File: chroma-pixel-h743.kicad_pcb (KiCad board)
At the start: 6 copper layers, 76 x 78 mm, 136 parts, among them J1 Micro_SD_Card_Det_Hirose_DM3AT, J2 TFT_LCD, J4 USB-C, J5 I2C-STEMMA-QT, J6 BAT, J7 swd, J8 SPKR, J9 UART, SW1 SW_Push, SW2 SW_Push, SW3 SW_Push, SW4 SW_Push, U1 MT25Q, U10 STM32H743ZITx, U11 MT48LC16M16A2P, U5 TPS61169, U6 MAX98357AETE_, U7 CAT24C128, U8 TLV75733PDBV, U9 W25Q128JVS, Y1 25MHz, Y2 32.768KHz

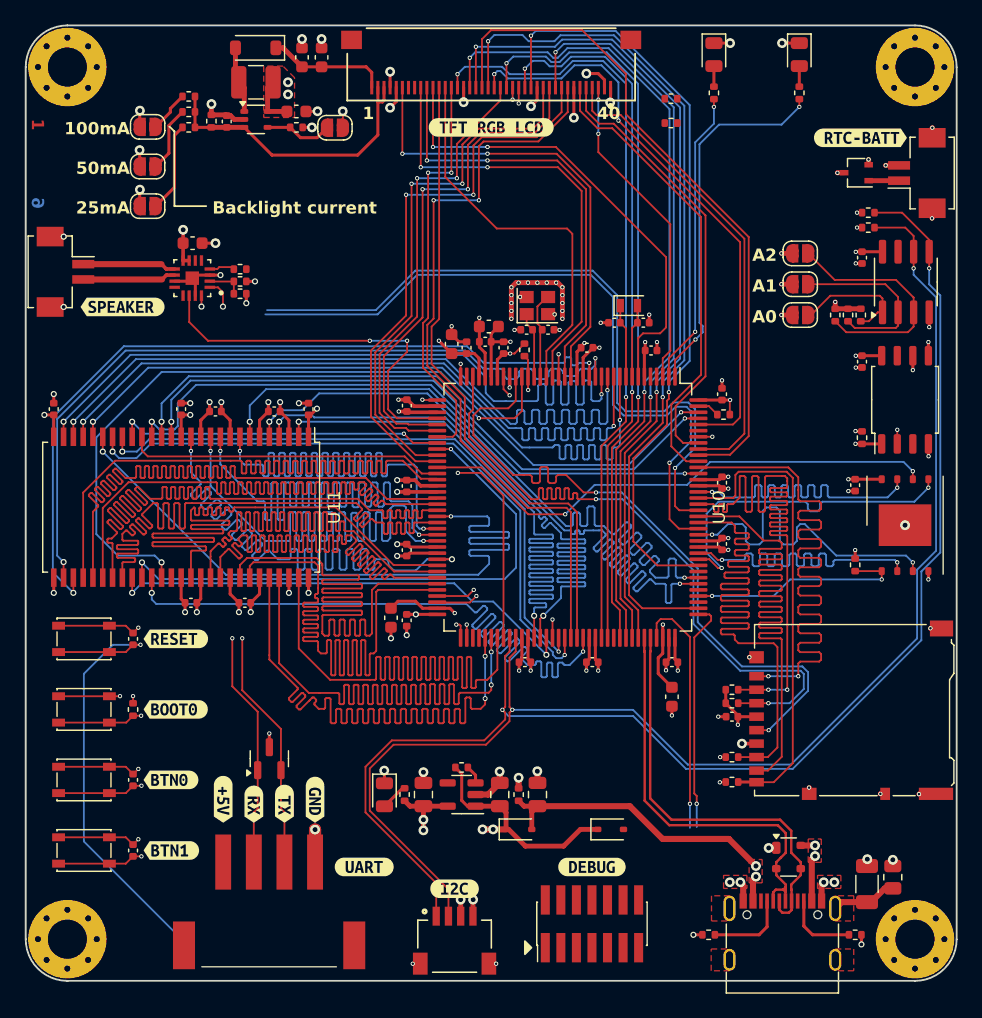
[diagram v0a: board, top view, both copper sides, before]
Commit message: LTDC route almost finished
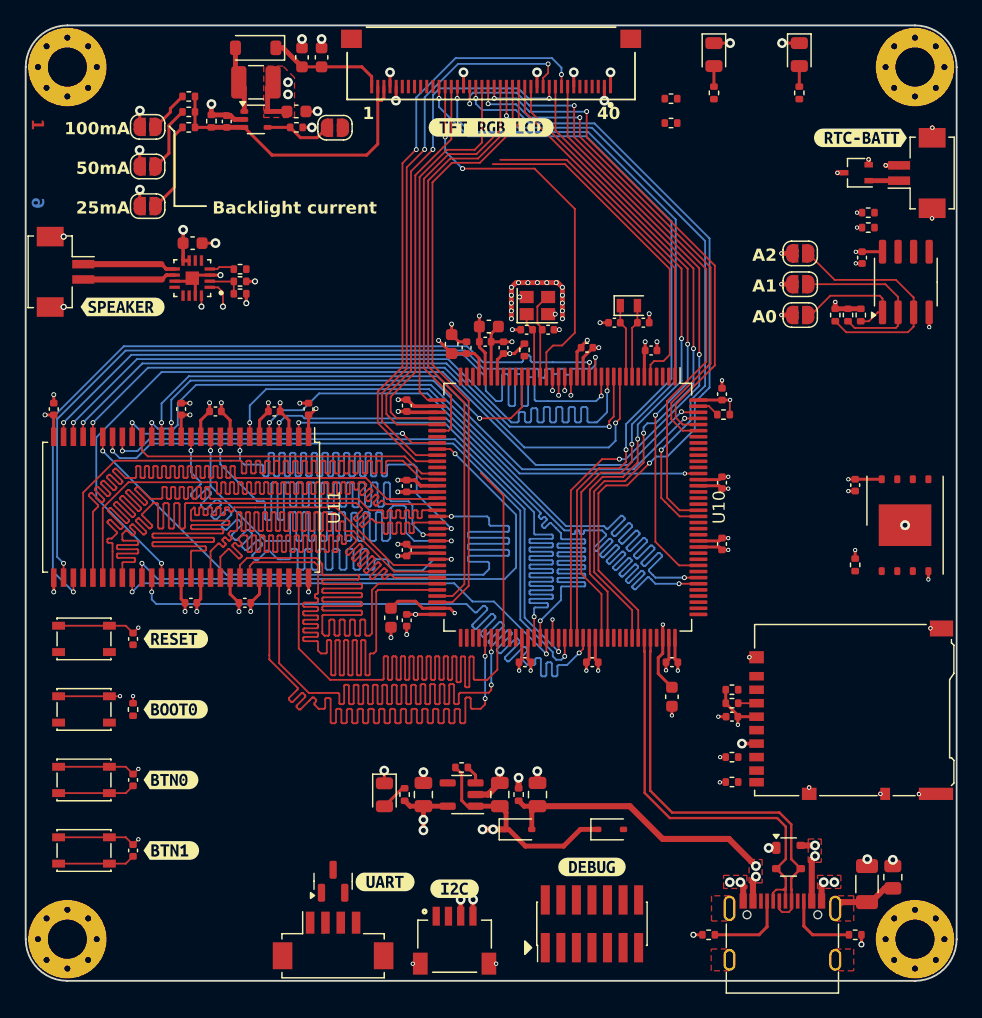
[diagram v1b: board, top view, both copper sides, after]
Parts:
- removed C22: 100n, Capacitor_SMD:C_0402_1005Metric
- removed R1: 10K, Resistor_SMD:R_0402_1005Metric
- removed U9: W25Q128JVS, Package_SO:SOIC-8_5.23x5.23mm_P1.27mm
- removed kibuzzard-664329E8: G***, kibuzzard-664329E8
- removed kibuzzard-664329F6: G***, kibuzzard-664329F6
- removed kibuzzard-6644A120: G***, kibuzzard-6644A120
- removed kibuzzard-6644A126: G***, kibuzzard-6644A126
- J9: footprint S4B-XH-SM4-TB_LF__SN:S4BXHSM4TBLFSN -> Connector_Hirose:Hirose_DF13C_CL535-0404-8-51_1x04-1MP_P1.25mm_Vertical
- moved D9 11.3 mm to (131.3, 118.2)
- moved J9 5.64 mm to (131.3, 123.0)
- moved kibuzzard-6642BE54 2.09 mm to (135.5, 118.3)
- moved J2 0.09 mm to (144.2, 51.4)
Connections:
- net /MCU/I2S_CK renamed /Audio/I2S_CK
- net /MCU/I2S_SDO renamed /Audio/I2S_SDO
- net /MCU/I2S_SD_MODE renamed /Audio/I2S_SD_MODE
- net /MCU/I2S_WS renamed /Audio/I2S_WS
- net /MCU/PC0 renamed /MCU/~{SDRAM_WE}
- net /MCU/PC4 renamed /MCU/~{SDRAM_CS}
- net /MCU/PC5 renamed /MCU/SDRAM_CKE
- net /MCU/PE0 renamed /MCU/SDRAM_LDQM
- net /MCU/PE1 renamed /MCU/SDRAM_UDQM
- net /MCU/PF11 renamed /MCU/~{SDRAM_RAS}
- net /MCU/PG15 renamed /MCU/~{SDRAM_CAS}
- net /MCU/PG4 renamed /MCU/SDRAM_BA0
- net /MCU/PG5 renamed /MCU/SDRAM_BA1
- net /MCU/PG8 renamed /MCU/SDRAM_CLK
- R2 pad 2: /MCU/~{NOR_CS} -> /MEMORY/~{NOR_CS}
- U1 pad 1: /MCU/~{NOR_CS} -> /MEMORY/~{NOR_CS}
- U1 pad 2: /MCU/NOR_D1 -> /MEMORY/NOR_DO(IO1)
- U1 pad 3: /MCU/NOR_D2 -> /MEMORY/NOR_IO2
- U1 pad 5: /MCU/NOR_D0 -> /MEMORY/NOR_DI(IO0)
- U1 pad 6: /MCU/NOR_CLK -> /MEMORY/NOR_CLK
- U1 pad 7: /MCU/NOR_D3 -> /MEMORY/NOR_IO3
- U10 pad 1: unconnected-(U10-PE2-Pad1) -> /LCD/LCD_SPI_CLK
- U10 pad 101: unconnected-(U10-PA9-Pad101) -> /LCD/LCD_R5
- U10 pad 102: unconnected-(U10-PA10-Pad102) -> /LCD/LCD_B4
- U10 pad 103: unconnected-(U10-PA11-Pad103) -> /MCU/USB_D-
- U10 pad 104: unconnected-(U10-PA12-Pad104) -> /MCU/USB_D+
- U10 pad 117: unconnected-(U10-PD3-Pad117) -> /LCD/LCD_G7
- U10 pad 125: unconnected-(U10-PG10-Pad125) -> /LCD/LCD_G3
- U10 pad 126: unconnected-(U10-PG11-Pad126) -> /LCD/LCD_B3
- U10 pad 136: unconnected-(U10-PB6-Pad136) -> /MEMORY/~{NOR_CS}
- U10 pad 139: unconnected-(U10-PB8-Pad139) -> /LCD/LCD_B6
- U10 pad 140: unconnected-(U10-PB9-Pad140) -> /LCD/LCD_B7
- U10 pad 18: unconnected-(U10-PF6-Pad18) -> /MEMORY/NOR_IO3
- U10 pad 19: unconnected-(U10-PF7-Pad19) -> /MEMORY/NOR_IO2
- U10 pad 2: unconnected-(U10-PE3-Pad2) -> /LCD/LCD_SPI_CS
- U10 pad 20: unconnected-(U10-PF8-Pad20) -> /MEMORY/NOR_DI(IO0)
- U10 pad 21: unconnected-(U10-PF9-Pad21) -> /MEMORY/NOR_DO(IO1)
- U10 pad 22: unconnected-(U10-PF10-Pad22) -> /LCD/LCD_DE
- U10 pad 3: unconnected-(U10-PE4-Pad3) -> /LCD/LCD_RESET
- U10 pad 37: unconnected-(U10-PA3-Pad37) -> /LCD/LCD_B5
- U10 pad 40: unconnected-(U10-PA4-Pad40) -> /LCD/VSYNC
- U10 pad 41: unconnected-(U10-PA5-Pad41) -> /LCD/LCD_R4
- U10 pad 42: unconnected-(U10-PA6-Pad42) -> /LCD/LCD_G2
- U10 pad 43: unconnected-(U10-PA7-Pad43) -> /LCD/LCD_BLK
- U10 pad 46: unconnected-(U10-PB0-Pad46) -> /LCD/LCD_R3
- U10 pad 47: unconnected-(U10-PB1-Pad47) -> /LCD/LCD_R6
- U10 pad 48: unconnected-(U10-PB2-Pad48) -> /MEMORY/NOR_CLK
- U10 pad 5: unconnected-(U10-PE6-Pad5) -> /LCD/LCD_SPI_DAT
- U10 pad 69: unconnected-(U10-PB10-Pad69) -> /LCD/LCD_G4
- U10 pad 70: unconnected-(U10-PB11-Pad70) -> /LCD/LCD_G5
- U10 pad 91: unconnected-(U10-PG6-Pad91) -> /LCD/LCD_R7
- U10 pad 92: unconnected-(U10-PG7-Pad92) -> /LCD/LCD_CLK
- U10 pad 96: unconnected-(U10-PC6-Pad96) -> /LCD/HSYNC
- U10 pad 97: unconnected-(U10-PC7-Pad97) -> /LCD/LCD_G6
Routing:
- net /IO/STEMMA_SCL: track 114.3 -> 0.00 mm, vias 2 -> 0
- net /IO/STEMMA_SDA: track 111.8 -> 0.00 mm, vias 2 -> 0
- net /IO/NRST: track 89.2 -> 0.00 mm, vias 2 -> 0
- net /MCU/BOOT0: track 72.3 -> 0.00 mm, vias 2 -> 0
- net /IO/USART2_TX: track 62.3 -> 0.00 mm, vias 2 -> 0
- net /MCU/SD_DAT0: track 60.5 -> 0.00 mm
- net /IO/USART2_RX: track 60.4 -> 0.00 mm, vias 2 -> 0
- net /MCU/SD_DAT3: track 59.9 -> 0.00 mm, vias 2 -> 0
- net /MCU/SD_DAT1: track 59.0 -> 0.00 mm
- net unconnected-(U10-PD7-Pad123): track 58.7 -> 0.00 mm, vias 1 -> 0
- net /MCU/SD_DAT2: track 58.4 -> 0.00 mm, vias 2 -> 0
- net /MCU/SPI_CLK: track 58.3 -> 0.00 mm, vias 2 -> 0
- net unconnected-(U10-PG11-Pad126): track 57.4 -> 0.00 mm, vias 1 -> 0
- net /MCU/SD_CMD: track 57.4 -> 1.50 mm, vias 2 -> 0
- net /MCU/SD_CLK: track 55.9 -> 0.00 mm, vias 2 -> 0
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
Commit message: Added chroma pixel png
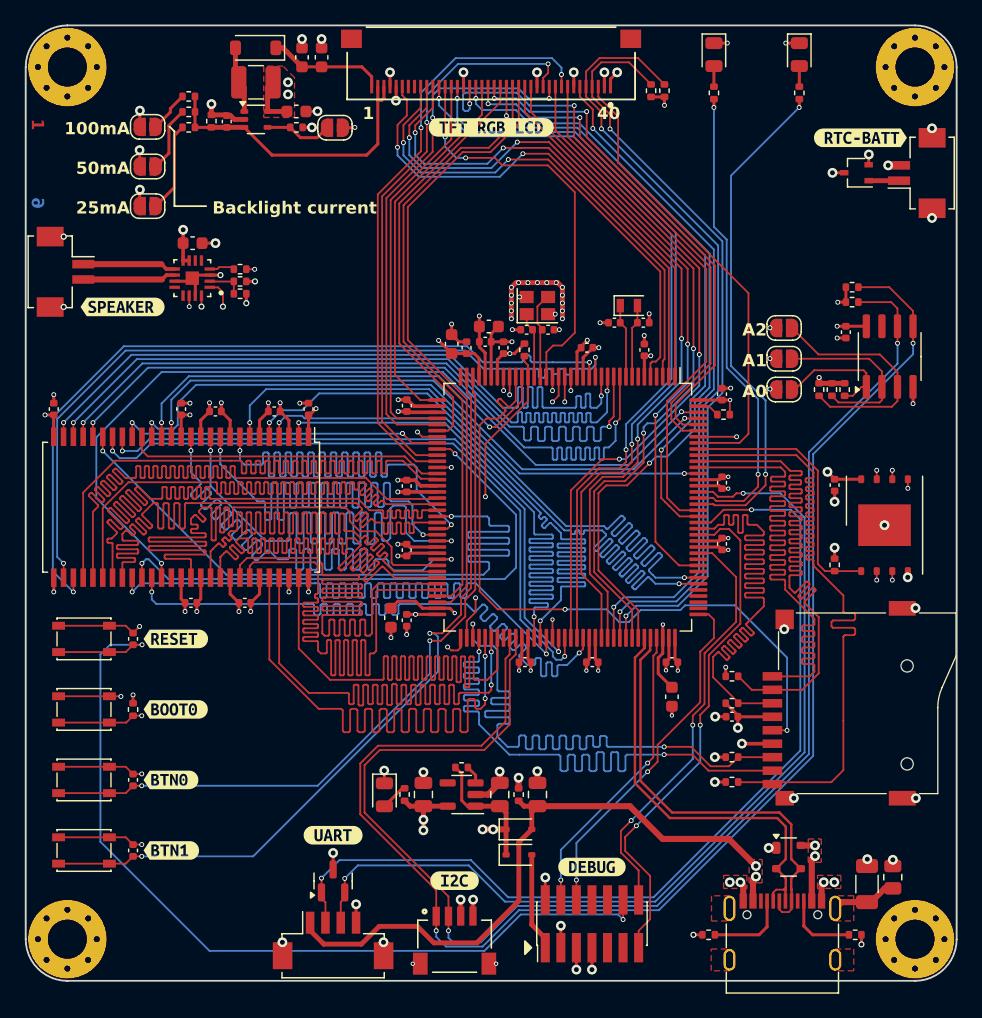
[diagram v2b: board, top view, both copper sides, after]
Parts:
- removed J1: Micro_SD_Card_Det_Hirose_DM3AT, Connector_Card:microSD_HC_Hirose_DM3AT-SF-PEJM5
- added J3: Micro_SD_Card_Det1, TF-115:SD-TF-115, F.Cu at (172.4, 103.7)
- moved D10 7.77 mm to (146.5, 116.1)
- moved C20 6.23 mm to (173.2, 73.4)
- moved JP6 6.23 mm to (168.1, 75.6)
- moved JP7 6.23 mm to (168.1, 78.1)
- moved R30 6.23 mm to (173.1, 78.1)
- moved R31 6.23 mm to (172.0, 78.1)
- moved R32 6.23 mm to (171.0, 78.1)
- moved R6 6.23 mm to (173.7, 70.9)
- moved U7 6.23 mm to (176.7, 75.4)
- moved JP5 6.23 mm to (168.1, 73.0)
- moved R5 6.23 mm to (173.7, 69.7)
- moved kibuzzard-6642BE54 5.70 mm to (131.3, 114.5)
- moved R34 3.10 mm to (157.3, 53.7), turned to 90 degrees
- moved C21 1.68 mm to (172.2, 85.9)
- moved R2 1.68 mm to (172.2, 92.4)
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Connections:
- D9 pad 1: /IO/USART2_RX -> /IO/EXT_RX
- D9 pad 2: /IO/USART2_TX -> /IO/EXT_TX
- J7 pad 13: /IO/USART1_RX -> /IO/DBG_USART_RX
- J7 pad 14: /IO/USART1_TX -> /IO/DBG_USART_TX
- J9 pad 1: +5V -> VBUS
- J9 pad 2: /IO/USART2_RX -> /IO/EXT_RX
- J9 pad 3: /IO/USART2_TX -> /IO/EXT_TX
- R10 pad 1: /MCU/PG13 -> /MEMORY/SD_DET
- R7 pad 2: /MCU/SD_DAT0 -> /MEMORY/SD_DAT0
- R8 pad 2: /MCU/SD_CMD -> /MEMORY/SD_CMD
- R9 pad 2: /MCU/SD_DAT3 -> /MEMORY/SD_DAT3/CD
- U10 pad 100: unconnected-(U10-PA8-Pad100) -> /LCD/LCD_TP_SCL
- U10 pad 119: unconnected-(U10-PD5-Pad119) -> /IO/DBG_USART_TX
- U10 pad 122: unconnected-(U10-PD6-Pad122) -> /IO/DBG_USART_RX
- U10 pad 123: unconnected-(U10-PD7-Pad123) -> /MEMORY/SD_CMD
- U10 pad 124: unconnected-(U10-PG9-Pad124) -> /IO/EXT_RX
- U10 pad 127: unconnected-(U10-PG12-Pad127) -> /MCU/LED_0
- U10 pad 128: unconnected-(U10-PG13-Pad128) -> /MCU/LED_1
- U10 pad 129: unconnected-(U10-PG14-Pad129) -> /IO/EXT_TX
- U10 pad 133: unconnected-(U10-PB3-Pad133) -> /MEMORY/SD_DAT2
- U10 pad 134: unconnected-(U10-PB4-Pad134) -> /MEMORY/SD_DAT3/CD
- U10 pad 135: unconnected-(U10-PB5-Pad135) -> /MEMORY/SD_DET
- U10 pad 137: unconnected-(U10-PB7-Pad137) -> /LCD/LCD_TP_RST
- U10 pad 27: unconnected-(U10-PC1-Pad27) -> /MEMORY/SD_CLK
- U10 pad 28: unconnected-(U10-PC2_C-Pad28) -> /Audio/I2S_SD_MODE
- U10 pad 29: unconnected-(U10-PC3_C-Pad29) -> /Audio/I2S_SDO
- U10 pad 34: unconnected-(U10-PA0-Pad34) -> /MCU/BTN0
- U10 pad 35: unconnected-(U10-PA1-Pad35) -> /MCU/BTN1
- U10 pad 73: unconnected-(U10-PB12-Pad73) -> /Audio/I2S_WS
- U10 pad 74: unconnected-(U10-PB13-Pad74) -> /Audio/I2S_CK
- U10 pad 75: unconnected-(U10-PB14-Pad75) -> /MEMORY/SD_DAT0
- U10 pad 76: unconnected-(U10-PB15-Pad76) -> /MEMORY/SD_DAT1
- U10 pad 81: unconnected-(U10-PD12-Pad81) -> /IO/STEMMA_SCL
- U10 pad 82: unconnected-(U10-PD13-Pad82) -> /IO/STEMMA_SDA
- U10 pad 98: unconnected-(U10-PC8-Pad98) -> /LCD/LCD_TP_INT
- U10 pad 99: unconnected-(U10-PC9-Pad99) -> /LCD/LCD_TP_SDA
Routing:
- net /IO/NRST: track 0.00 -> 135.1 mm, vias 0 -> 3
- net /IO/STEMMA_SCL: track 0.00 -> 119.5 mm, vias 0 -> 2
- net /IO/STEMMA_SDA: track 0.00 -> 116.2 mm, vias 0 -> 2
- net /MCU/BOOT0: track 0.00 -> 92.0 mm, vias 0 -> 2
- net /IO/EXT_RX: track 0.00 -> 77.6 mm, vias 0 -> 2
- net /IO/EXT_TX: track 0.00 -> 76.9 mm, vias 0 -> 2
- net /LCD/LCD_TP_SDA: track 0.00 -> 64.0 mm, vias 0 -> 2
- net /LCD/LCD_TP_SCL: track 0.00 -> 61.8 mm, vias 0 -> 2
- net /MEMORY/SD_DET: track 0.00 -> 60.0 mm
- net /MEMORY/SD_CMD: track 0.00 -> 60.0 mm
- net /MEMORY/SD_DAT2: track 0.00 -> 60.0 mm
- net /MEMORY/SD_DAT3/CD: track 0.00 -> 60.0 mm
- net /MCU/BTN1: track 6.33 -> 64.2 mm, vias 0 -> 2
- net /MEMORY/SD_DAT0: track 0.00 -> 56.9 mm, vias 0 -> 2
- net /MEMORY/SD_DAT1: track 0.00 -> 56.9 mm, vias 0 -> 2
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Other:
- board text added: "5V"
- board text added: "GND"
- board text added: "RX"
- board text added: "SCL"
- board text added: "SDA"
- board text added: "TX"
- board text added: "VDD"

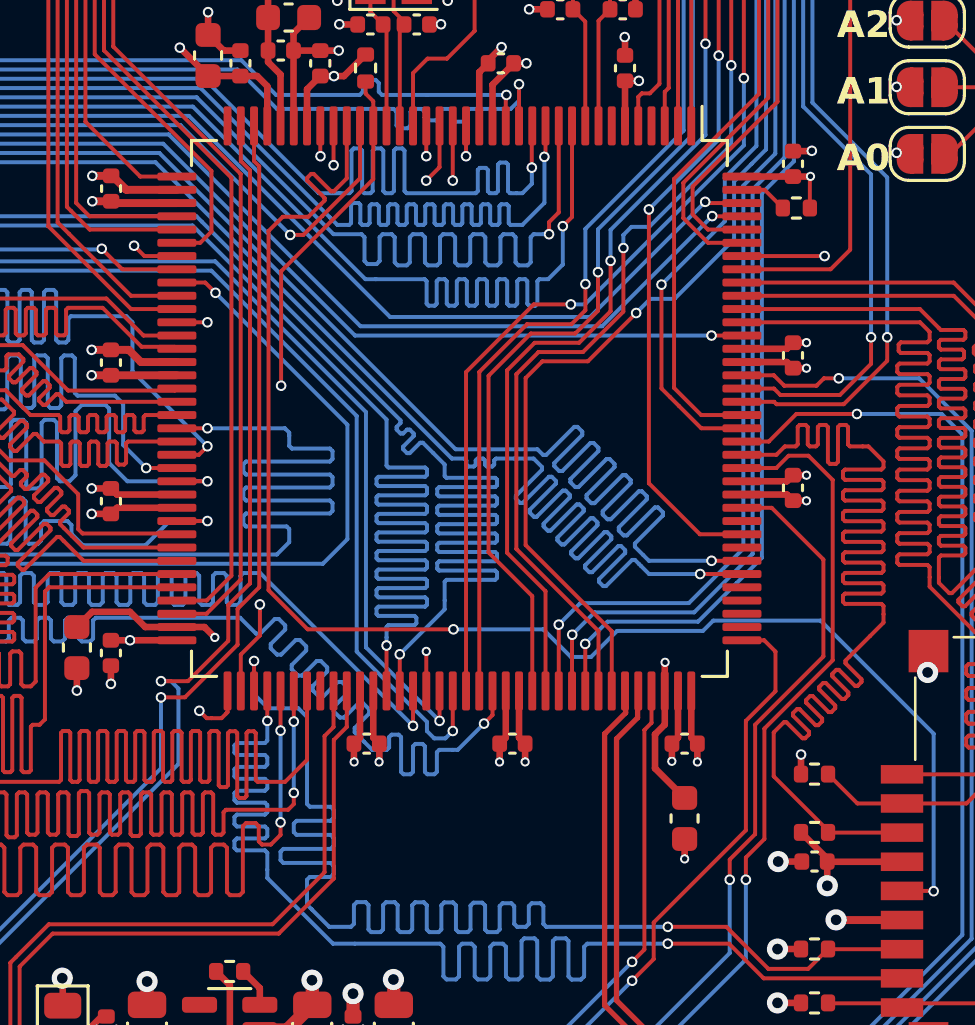
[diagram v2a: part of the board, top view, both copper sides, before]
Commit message: Fix to small via
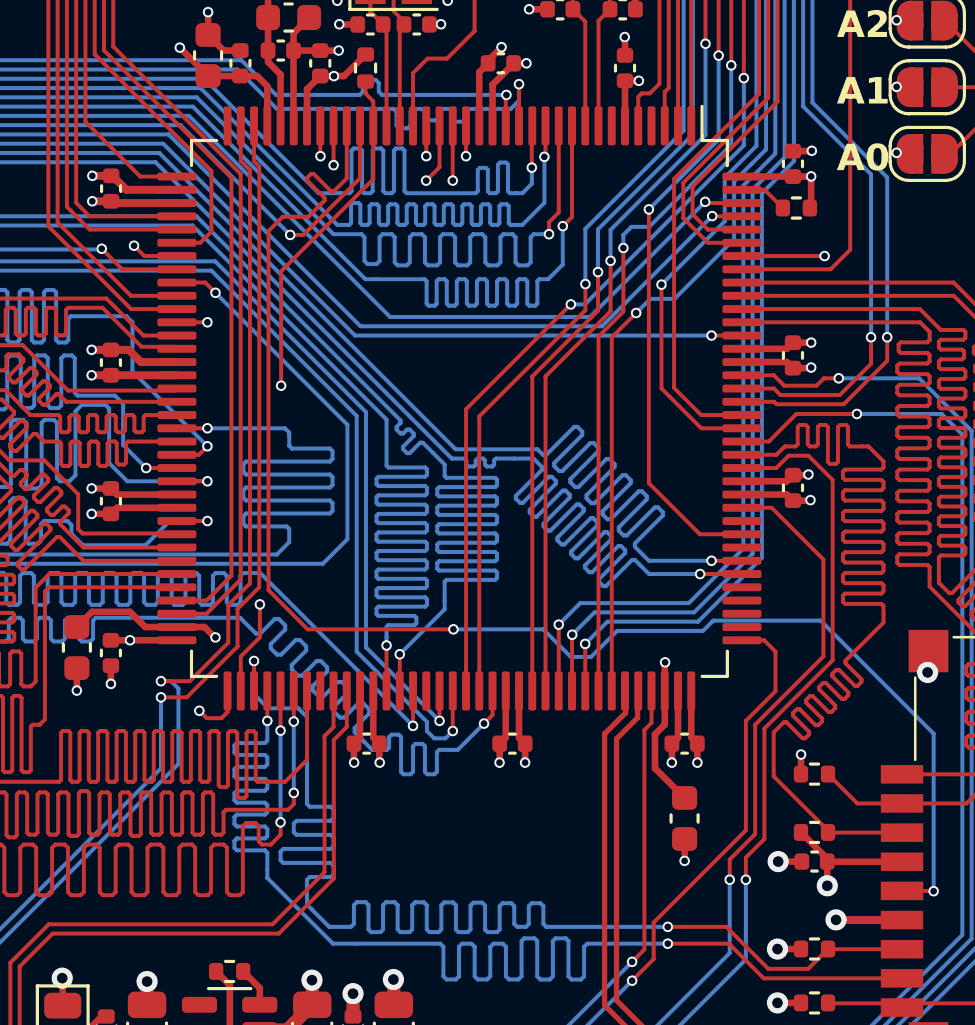
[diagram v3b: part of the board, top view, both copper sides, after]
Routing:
- net /LCD/LCD_B4: track 63.6 -> 59.9 mm
- net /LCD/LCD_R5: track 55.7 -> 52.1 mm
- net unconnected-(U10-PG3-Pad88): track 2.55 -> 0.00 mm, vias 1 -> 0
- net /LCD/HSYNC: track 62.2 -> 59.9 mm
- net /LCD/LCD_G6: track 55.0 -> 52.8 mm
- net /LCD/LCD_CLK: track 62.0 -> 61.0 mm
- net /LCD/LCD_R7: track 54.9 -> 54.1 mm
- net GND: track 161.1 -> 161.7 mm

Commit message: First release H743 version
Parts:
- added G***: LOGO, logo:chroma-pixel, F.Cu at (144.9, 64.5)
- D7: footprint Package_TO_SOT_SMD:SOT-323_SC-70 -> Package_TO_SOT_SMD:SOT-23
- R16: value NC -> 100K
- moved D7 0.53 mm to (173.5, 60.4)
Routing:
- net /IO/SWDIO: track 24.6 -> 29.9 mm
- net /IO/SWCLK: track 29.0 -> 29.9 mm
- net VB: track 2.48 -> 3.20 mm
- net +3V3: track 104.6 -> 105.2 mm
- net GND: track 161.7 -> 162.2 mm
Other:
- board text added: "."
- board text added: "LED0"
- board text added: "LED1"
- board text added: "W"
